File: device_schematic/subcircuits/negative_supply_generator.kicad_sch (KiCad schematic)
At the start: 4 parts, among them U1 ICL7660S

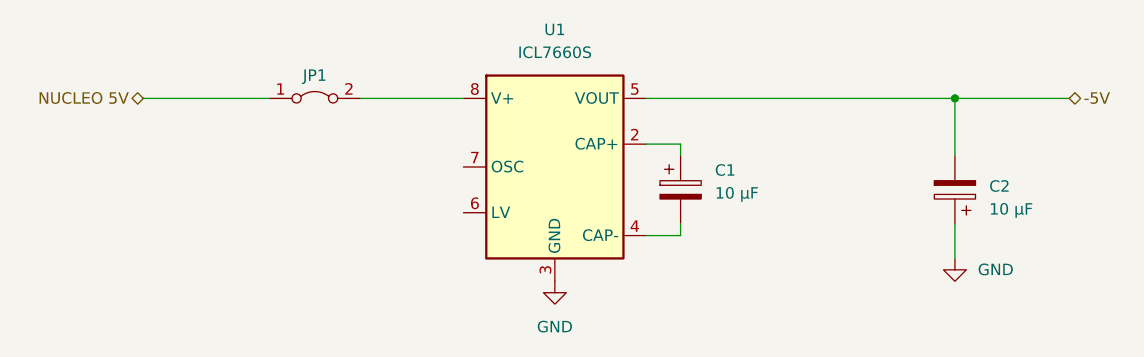
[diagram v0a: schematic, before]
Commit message: Device schematic finished version
+ correction to use D7 in place of D13
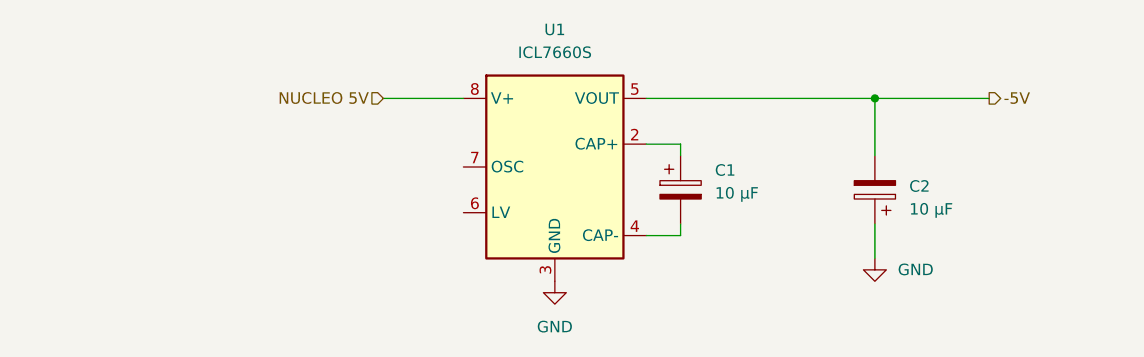
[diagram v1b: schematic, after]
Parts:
- removed JP1: (no value), symbol Jumper:Jumper_2_Bridged
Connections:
- net NUCLEO 5V: now also U1.8 (V+)
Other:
- moved on the sheet: C2
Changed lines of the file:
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@@
 (kicad_sch (version 20211123) (generator eeschema)
   (paper "A4")
-  (junction (at 177.8 91.44) (diameter 0) (color 0 0 0 0)
+  (junction (at 168.91 91.44) (diameter 0) (color 0 0 0 0)
   )
-  (wire (pts (xy 87.63 91.44) (xy 101.6 91.44))
+  (wire (pts (xy 114.3 91.44) (xy 123.19 91.44))
     (stroke (width 0) (type default) (color 0 0 0 0))
   )
   (wire (pts (xy 147.32 105.41) (xy 147.32 106.68))
+    (stroke (width 0) (type default) (color 0 0 0 0))
+  )
+  (wire (pts (xy 143.51 91.44) (xy 168.91 91.44))
     (stroke (width 0) (type default) (color 0 0 0 0))
   )
@@
     (stroke (width 0) (type default) (color 0 0 0 0))
   )
-  (wire (pts (xy 177.8 105.41) (xy 177.8 109.22))
+  (wire (pts (xy 168.91 105.41) (xy 168.91 109.22))
     (stroke (width 0) (type default) (color 0 0 0 0))
   )
@@
     (stroke (width 0) (type default) (color 0 0 0 0))
   )
-  (wire (pts (xy 143.51 91.44) (xy 177.8 91.44))
+  (wire (pts (xy 168.91 91.44) (xy 168.91 97.79))
     (stroke (width 0) (type default) (color 0 0 0 0))
   )
-  (wire (pts (xy 111.76 91.44) (xy 123.19 91.44))
+  (wire (pts (xy 168.91 91.44) (xy 181.61 91.44))
     (stroke (width 0) (type default) (color 0 0 0 0))
   )
-  (wire (pts (xy 177.8 91.44) (xy 177.8 97.79))
-    (stroke (width 0) (type default) (color 0 0 0 0))
-  )
-  (wire (pts (xy 177.8 91.44) (xy 190.5 91.44))
-    (stroke (width 0) (type default) (color 0 0 0 0))
-  )
-  (hierarchical_label "-5V" (shape bidirectional) (at 190.5 91.44 0)
+  (hierarchical_label "-5V" (shape output) (at 181.61 91.44 0)
     (effects (font (size 1.27 1.27)) (justify left))
   )
-  (hierarchical_label "NUCLEO 5V" (shape bidirectional) (at 87.63 91.44 180)
+  (hierarchical_label "NUCLEO 5V" (shape input) (at 114.3 91.44 180)
     (effects (font (size 1.27 1.27)) (justify right))
   )
@@
     (pin "1")
   )
-  (symbol (lib_id "Device:C_Polarized") (at 177.8 101.6 180) (unit 1)
+  (symbol (lib_id "Device:C_Polarized") (at 168.91 101.6 180) (unit 1)
     (in_bom yes) (on_board yes) (fields_autoplaced)
-    (property "Reference" "C2" (id 0) (at 181.61 101.2189 0)
+    (property "Reference" "C2" (id 0) (at 172.72 101.2189 0)
       (effects (font (size 1.27 1.27)) (justify right))
     )
-    (property "Value" "10 µF" (id 1) (at 181.61 103.7589 0)
-      (effects (font (size 0 0)) (justify right))
+    (property "Value" "10 µF" (id 1) (at 172.72 103.7589 0)
+      (effects (font (size 1.27 1.27)) (justify right))
     )
-    (property "Footprint" "" (id 2) (at 176.8348 97.79 0)
+    (property "Footprint" "" (id 2) (at 167.9448 97.79 0)
       (effects (font (size 0 0)) hide)
     )
-    (property "Datasheet" "~" (id 3) (at 177.8 101.6 0)
+    (property "Datasheet" "~" (id 3) (at 168.91 101.6 0)
       (effects (font (size 1.27 1.27)) hide)
     )
@@
     (pin "2")
   )
-  (symbol (lib_id "power:GND") (at 177.8 109.22 0) (unit 1)
+  (symbol (lib_id "power:GND") (at 168.91 109.22 0) (unit 1)
     (in_bom yes) (on_board yes) (fields_autoplaced)
-    (property "Reference" "#PWR?" (id 0) (at 177.8 115.57 0)
+    (property "Reference" "#PWR?" (id 0) (at 168.91 115.57 0)
       (effects (font (size 1.27 1.27)) hide)
     )
-    (property "Value" "GND" (id 1) (at 180.34 110.4899 0)
+    (property "Value" "GND" (id 1) (at 171.45 110.4899 0)
       (effects (font (size 1.27 1.27)) (justify left))
     )
-    (property "Footprint" "" (id 2) (at 177.8 109.22 0)
+    (property "Footprint" "" (id 2) (at 168.91 109.22 0)
       (effects (font (size 1.27 1.27)) hide)
     )
-    (property "Datasheet" "" (id 3) (at 177.8 109.22 0)
+    (property "Datasheet" "" (id 3) (at 168.91 109.22 0)
       (effects (font (size 1.27 1.27)) hide)
     )
     (pin "1")
   )
-  (symbol (lib_id "Jumper:Jumper_2_Bridged") (at 106.68 91.44 0) (unit 1)
-    (in_bom yes) (on_board yes)
-    (property "Reference" "JP1" (id 0) (at 106.68 88.9 0))
-    (property "Value" "" (id 1) (at 106.68 87.63 0)
-      (effects (font (size 0 0)) hide)
-    )
-    (property "Footprint" "" (id 2) (at 106.68 91.44 0)
-      (effects (font (size 1.27 1.27)) hide)
-    )
-    (property "Datasheet" "~" (id 3) (at 106.68 91.44 0)
-      (effects (font (size 1.27 1.27)) hide)
-    )
-    (pin "1")
-    (pin "2")
-  )
 )
